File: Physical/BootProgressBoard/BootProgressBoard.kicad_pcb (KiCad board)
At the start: 2 copper layers, 67.5 x 28.6 mm, 15 parts, among them P1 CONN_01X09

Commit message: Latest version
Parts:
- moved G*** 18.5 mm to (154.4, 61.7)
- moved G*** 18.5 mm to (99.3, 61.7)
- moved P1 5.08 mm to (144.8, 59.7)
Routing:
- net Net-(D1-Pad2): track 23.0 -> 17.9 mm
- net Net-(D2-Pad2): track 16.8 -> 11.8 mm
- net Net-(D8-Pad2): track 7.40 -> 11.9 mm
- net Net-(D7-Pad2): track 6.35 -> 10.2 mm
- net Net-(P1-Pad1): track 45.2 -> 48.9 mm
- net Net-(D3-Pad2): track 13.6 -> 11.1 mm
- net Net-(D4-Pad2): track 11.0 -> 8.67 mm
- net Net-(D6-Pad2): track 7.40 -> 8.67 mm
- net Net-(D5-Pad2): track 8.45 -> 7.62 mm
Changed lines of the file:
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@@
     (thickness 1.6)
     (drawings 13)
-    (tracks 55)
+    (tracks 67)
     (zones 0)
     (modules 15)
@@
   )
   (module "MCQN Ltd:miab-logo-9x7mm" (layer B.Cu)
-    (at 154.432 43.18 180)
+    (at 154.432 61.722 180)
     (fp_text reference G*** (at 0 0 180) (layer B.SilkS) hide
       (effects (font (thickness 0.3)) (justify mirror))
@@
   )
   (module Socket_Strips:Socket_Strip_Straight_1x09 (layer F.Cu)
-    (at 149.86 59.69 180)
+    (at 144.78 59.69 180)
     (descr "Through hole socket strip")
     (tags "socket strip")
@@
   )
   (module "MCQN Ltd:miab-logo-9x7mm" (layer F.Cu)
-    (at 99.314 43.18)
+    (at 99.314 61.722)
     (fp_text reference G*** (at 0 0) (layer F.SilkS) hide
       (effects (font (thickness 0.3)))
@@
     (effects (font (size 1.5 1.5) (thickness 0.3)))
   )
-  (gr_text GND (at 154.432 59.69) (layer F.SilkS)
+  (gr_text GND (at 149.098 59.182) (layer F.SilkS)
     (effects (font (size 1.5 1.5) (thickness 0.3)))
   )
@@
     (effects (font (size 1.5 1.5) (thickness 0.3)))
   )
-  (gr_text bpb20170406 (at 99.822 64.262) (layer F.SilkS)
+  (gr_text bpb20170406 (at 153.924 61.976) (layer F.SilkS)
     (effects (font (size 1 1) (thickness 0.25)))
   )
@@
   (gr_line (start 160.67 39.1) (end 160.67 65.675) (layer Edge.Cuts) (width 0.15))
   (gr_line (start 94.14 38.1) (end 159.67 38.1) (layer Edge.Cuts) (width 0.15))
-  (segment (start 129.54 59.69) (end 115.57 59.69) (width 0.3) (layer F.Cu) (net 1))
-  (segment (start 115.57 59.69) (end 109.22 53.34) (width 0.3) (layer F.Cu) (net 1))
+  (segment (start 124.46 59.69) (end 115.57 59.69) (width 0.3) (layer F.Cu) (net 1))
+  (segment (start 115.57 59.69) (end 114.3 58.42) (width 0.3) (layer F.Cu) (net 1))
+  (segment (start 114.3 58.42) (end 109.22 53.34) (width 0.3) (layer F.Cu) (net 1))
   (segment (start 106.8 43.18) (end 106.8 53.22) (width 0.3) (layer F.Cu) (net 2))
   (segment (start 106.8 53.22) (end 106.68 53.34) (width 0.3) (layer F.Cu) (net 2))
@@
   (segment (start 129.54 45.72) (end 129.54 45.8724) (width 0.3) (layer F.Cu) (net 3))
   (segment (start 129.54 45.8724) (end 127.1524 48.26) (width 0.3) (layer F.Cu) (net 3))
-  (segment (start 132.08 59.69) (end 129.54 57.15) (width 0.3) (layer F.Cu) (net 4))
-  (segment (start 129.54 57.15) (end 120.65 57.15) (width 0.3) (layer F.Cu) (net 4))
-  (segment (start 120.65 57.15) (end 119.38 55.88) (width 0.3) (layer F.Cu) (net 4))
+  (segment (start 127 59.69) (end 127 59.5376) (width 0.3) (layer F.Cu) (net 4))
+  (segment (start 127 59.5376) (end 124.968 57.5056) (width 0.3) (layer F.Cu) (net 4))
+  (segment (start 124.968 57.5056) (end 121.0056 57.5056) (width 0.3) (layer F.Cu) (net 4))
+  (segment (start 121.0056 57.5056) (end 119.38 55.88) (width 0.3) (layer F.Cu) (net 4))
   (segment (start 119.38 55.88) (end 119.38 53.34) (width 0.3) (layer F.Cu) (net 4))
   (segment (start 125.73 49.53) (end 121.92 53.34) (width 0.3) (layer F.Cu) (net 5))
@@
   (segment (start 132.08 45.8724) (end 128.4224 49.53) (width 0.3) (layer F.Cu) (net 5))
   (segment (start 132.08 45.72) (end 132.08 45.8724) (width 0.3) (layer F.Cu) (net 5))
+  (segment (start 129.54 59.69) (end 129.54 58.374) (width 0.3) (layer F.Cu) (net 6))
+  (segment (start 129.54 58.374) (end 127.554 56.388) (width 0.3) (layer F.Cu) (net 6))
+  (segment (start 125.476 56.388) (end 124.46 55.372) (width 0.3) (layer F.Cu) (net 6))
+  (segment (start 127.554 56.388) (end 125.476 56.388) (width 0.3) (layer F.Cu) (net 6))
+  (segment (start 124.46 55.372) (end 124.46 53.34) (width 0.3) (layer F.Cu) (net 6))
+  (segment (start 129.54 59.69) (end 129.54 59.5376) (width 0.3) (layer F.Cu) (net 6))
   (segment (start 124.46 54.61) (end 124.46 53.34) (width 0.3) (layer F.Cu) (net 6))
-  (segment (start 125.73 55.88) (end 124.46 54.61) (width 0.3) (layer F.Cu) (net 6))
-  (segment (start 129.54 55.88) (end 125.73 55.88) (width 0.3) (layer F.Cu) (net 6))
-  (segment (start 130.81 57.15) (end 129.54 55.88) (width 0.3) (layer F.Cu) (net 6))
-  (segment (start 132.2324 57.15) (end 130.81 57.15) (width 0.3) (layer F.Cu) (net 6))
-  (segment (start 134.62 59.69) (end 134.62 59.5376) (width 0.3) (layer F.Cu) (net 6))
-  (segment (start 134.62 59.5376) (end 132.2324 57.15) (width 0.3) (layer F.Cu) (net 6))
   (segment (start 134.62 45.72) (end 134.62 45.8724) (width 0.3) (layer F.Cu) (net 7))
   (segment (start 134.62 45.8724) (end 127.1524 53.34) (width 0.3) (layer F.Cu) (net 7))
   (segment (start 127.1524 53.34) (end 127 53.34) (width 0.3) (layer F.Cu) (net 7))
-  (segment (start 133.35 55.88) (end 137.16 59.69) (width 0.3) (layer F.Cu) (net 8))
-  (segment (start 130.81 55.88) (end 133.35 55.88) (width 0.3) (layer F.Cu) (net 8))
-  (segment (start 129.54 54.61) (end 130.81 55.88) (width 0.3) (layer F.Cu) (net 8))
+  (segment (start 132.08 59.69) (end 132.08 57.912) (width 0.3) (layer F.Cu) (net 8))
+  (segment (start 132.08 57.912) (end 129.54 55.372) (width 0.3) (layer F.Cu) (net 8))
+  (segment (start 129.54 55.372) (end 129.54 53.34) (width 0.3) (layer F.Cu) (net 8))
   (segment (start 129.54 53.34) (end 129.54 54.61) (width 0.3) (layer F.Cu) (net 8))
   (segment (start 137.16 45.72) (end 137.16 45.8724) (width 0.3) (layer F.Cu) (net 9))
   (segment (start 137.16 45.8724) (end 132.08 50.9524) (width 0.3) (layer F.Cu) (net 9))
   (segment (start 132.08 50.9524) (end 132.08 53.34) (width 0.3) (layer F.Cu) (net 9))
-  (segment (start 134.62 54.61) (end 139.7 59.69) (width 0.3) (layer F.Cu) (net 10))
+  (segment (start 134.62 59.69) (end 134.62 53.34) (width 0.3) (layer F.Cu) (net 10))
   (segment (start 134.62 53.34) (end 134.62 54.61) (width 0.3) (layer F.Cu) (net 10))
   (segment (start 137.16 50.8) (end 137.16 53.34) (width 0.3) (layer F.Cu) (net 11))
   (segment (start 139.7 48.26) (end 137.16 50.8) (width 0.3) (layer F.Cu) (net 11))
   (segment (start 139.7 45.72) (end 139.7 48.26) (width 0.3) (layer F.Cu) (net 11))
-  (segment (start 142.24 57.15) (end 142.24 59.69) (width 0.3) (layer F.Cu) (net 12))
-  (segment (start 139.7 54.61) (end 142.24 57.15) (width 0.3) (layer F.Cu) (net 12))
+  (segment (start 137.16 59.69) (end 137.16 57.658) (width 0.3) (layer F.Cu) (net 12))
+  (segment (start 137.16 57.658) (end 139.7 55.118) (width 0.3) (layer F.Cu) (net 12))
+  (segment (start 139.7 55.118) (end 139.7 53.34) (width 0.3) (layer F.Cu) (net 12))
   (segment (start 139.7 53.34) (end 139.7 54.61) (width 0.3) (layer F.Cu) (net 12))
   (segment (start 142.24 45.72) (end 142.24 53.34) (width 0.3) (layer F.Cu) (net 13))
-  (segment (start 144.78 53.34) (end 144.78 59.69) (width 0.3) (layer F.Cu) (net 14))
+  (segment (start 139.7 57.912) (end 140.716 56.896) (width 0.3) (layer F.Cu) (net 14))
+  (segment (start 140.716 56.896) (end 140.97 56.642) (width 0.3) (layer F.Cu) (net 14))
+  (segment (start 144.78 53.34) (end 144.78 55.118) (width 0.3) (layer F.Cu) (net 14))
+  (segment (start 144.78 55.118) (end 144.272 55.626) (width 0.3) (layer F.Cu) (net 14))
+  (segment (start 144.272 55.626) (end 141.986 55.626) (width 0.3) (layer F.Cu) (net 14))
+  (segment (start 141.986 55.626) (end 140.716 56.896) (width 0.3) (layer F.Cu) (net 14))
+  (segment (start 139.7 59.69) (end 139.7 57.912) (width 0.3) (layer F.Cu) (net 14))
   (segment (start 147.32 50.8) (end 147.32 53.34) (width 0.3) (layer F.Cu) (net 15))
   (segment (start 144.78 48.26) (end 147.32 50.8) (width 0.3) (layer F.Cu) (net 15))
   (segment (start 144.78 45.72) (end 144.78 48.26) (width 0.3) (layer F.Cu) (net 15))
-  (segment (start 147.32 57.15) (end 147.32 59.69) (width 0.3) (layer F.Cu) (net 16))
-  (segment (start 149.86 54.61) (end 147.32 57.15) (width 0.3) (layer F.Cu) (net 16))
-  (segment (start 149.86 53.34) (end 149.86 54.61) (width 0.3) (layer F.Cu) (net 16))
-  (segment (start 152.4 57.15) (end 149.86 59.69) (width 0.3) (layer F.Cu) (net 18))
-  (segment (start 152.4 48.26) (end 152.4 57.15) (width 0.3) (layer F.Cu) (net 18))
-  (segment (start 149.86 45.72) (end 152.4 48.26) (width 0.3) (layer F.Cu) (net 18))
-  (segment (start 147.32 45.72) (end 149.86 45.72) (width 0.3) (layer F.Cu) (net 18))
+  (segment (start 142.24 59.69) (end 142.24 58.166) (width 0.3) (layer F.Cu) (net 16))
+  (segment (start 142.24 58.166) (end 143.256 57.15) (width 0.3) (layer F.Cu) (net 16))
+  (segment (start 143.256 57.15) (end 147.32 57.15) (width 0.3) (layer F.Cu) (net 16))
+  (segment (start 147.32 57.15) (end 149.86 54.61) (width 0.3) (layer F.Cu) (net 16))
+  (segment (start 149.86 54.61) (end 149.86 53.34) (width 0.3) (layer F.Cu) (net 16))
+  (segment (start 144.78 59.69) (end 147.574 59.69) (width 0.3) (layer F.Cu) (net 18))
+  (segment (start 152.4 54.864) (end 152.4 48.26) (width 0.3) (layer F.Cu) (net 18))
+  (segment (start 147.574 59.69) (end 152.4 54.864) (width 0.3) (layer F.Cu) (net 18))
+  (segment (start 152.4 48.26) (end 149.86 45.72) (width 0.3) (layer F.Cu) (net 18))
+  (segment (start 149.86 45.72) (end 147.32 45.72) (width 0.3) (layer F.Cu) (net 18))
   (segment (start 144.78 43.18) (end 147.32 45.72) (width 0.3) (layer F.Cu) (net 18))
   (segment (start 121.8 43.18) (end 144.78 43.18) (width 0.3) (layer F.Cu) (net 18))

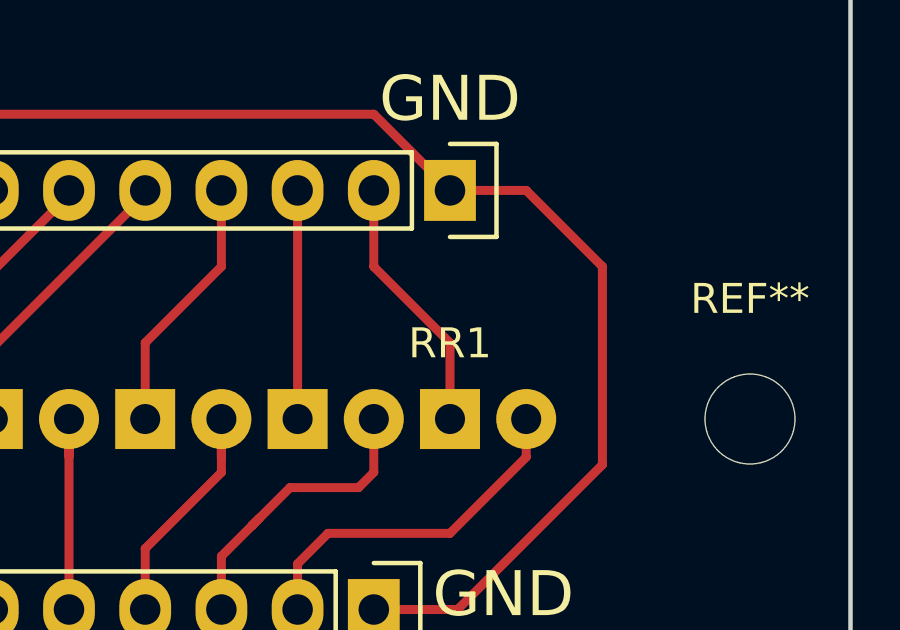
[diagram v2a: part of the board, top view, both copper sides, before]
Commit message: Add logo to the Boomer amp.  Part of #86
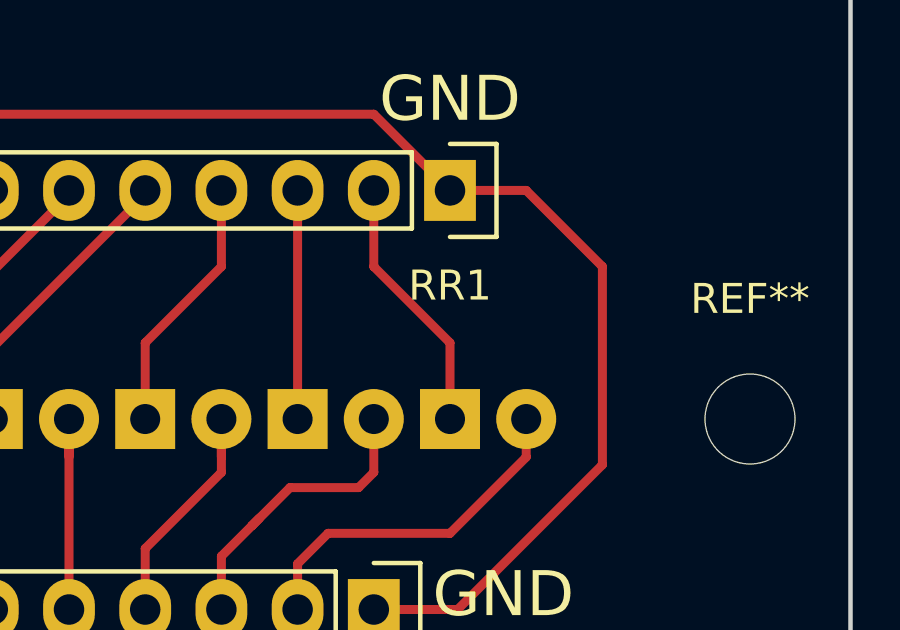
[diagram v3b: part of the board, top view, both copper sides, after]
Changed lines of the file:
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@@
-(kicad_pcb (version 20170123) (host pcbnew no-vcs-found-1e25c47~58~ubuntu16.04.1)
+(kicad_pcb (version 20171130) (host pcbnew 5.0.1-33cea8e~67~ubuntu18.04.1)
   (general
-    (links 18)
-    (no_connects 0)
-    (area 90.191475 38.024999 165.810046 66.750001)
     (thickness 1.6)
     (drawings 13)
@@
     (pad_drill 0.762)
     (pad_to_mask_clearance 0.2)
+    (solder_mask_min_width 0.25)
     (aux_axis_origin 0 0)
     (visible_elements FFFFFF7F)
@@
       (layerselection 0x010fc_ffffffff)
       (usegerberextensions false)
+      (usegerberattributes false)
+      (usegerberadvancedattributes false)
+      (creategerberjobfile false)
       (excludeedgelayer true)
       (linewidth 0.100000)
@@
       (hpglpennumber 1)
       (hpglpenspeed 20)
-      (hpglpendiameter 15)
+      (hpglpendiameter 15.000000)
       (psnegative false)
       (psa4output false)
@@
       (drillshape 0)
       (scaleselection 1)
-      (outputdirectory /home/adrian/sandbox/github/brain/Physical/BootProgressBoard/Output/))
+      (outputdirectory "/home/adrian/sandbox/github/brain/Physical/BootProgressBoard/Output/"))
   )
   (net 0 "")
@@
     (at 154.432 61.722 180)
     (fp_text reference G*** (at 0 0 180) (layer B.SilkS) hide
-      (effects (font (thickness 0.3)) (justify mirror))
+      (effects (font (size 1.524 1.524) (thickness 0.3)) (justify mirror))
     )
     (fp_text value LOGO (at 0.75 0 180) (layer B.SilkS) hide
-      (effects (font (thickness 0.3)) (justify mirror))
+      (effects (font (size 1.524 1.524) (thickness 0.3)) (justify mirror))
     )
     (fp_poly (pts (xy 4.611512 -3.293533) (xy -4.608688 -3.293533) (xy -4.608688 -1.255324) (xy -3.7846 -1.255324)
@@
       (net 4 "Net-(D2-Pad2)"))
     (model LEDs.3dshapes/LED-3MM.wrl
-      (at (xyz 0.05 0 0))
+      (offset (xyz 1.269999980926514 0 0))
       (scale (xyz 1 1 1))
       (rotate (xyz 0 0 90))
@@
       (net 6 "Net-(D3-Pad2)"))
     (model LEDs.3dshapes/LED-3MM.wrl
-      (at (xyz 0.05 0 0))
+      (offset (xyz 1.269999980926514 0 0))
       (scale (xyz 1 1 1))
       (rotate (xyz 0 0 90))
@@
       (net 8 "Net-(D4-Pad2)"))
     (model LEDs.3dshapes/LED-3MM.wrl
-      (at (xyz 0.05 0 0))
+      (offset (xyz 1.269999980926514 0 0))
       (scale (xyz 1 1 1))
       (rotate (xyz 0 0 90))
@@
       (net 10 "Net-(D5-Pad2)"))
     (model LEDs.3dshapes/LED-3MM.wrl
-      (at (xyz 0.05 0 0))
+      (offset (xyz 1.269999980926514 0 0))
       (scale (xyz 1 1 1))
       (rotate (xyz 0 0 90))
@@
       (net 12 "Net-(D6-Pad2)"))
     (model LEDs.3dshapes/LED-3MM.wrl
-      (at (xyz 0.05 0 0))
+      (offset (xyz 1.269999980926514 0 0))
       (scale (xyz 1 1 1))
       (rotate (xyz 0 0 90))
@@
       (net 14 "Net-(D7-Pad2)"))
     (model LEDs.3dshapes/LED-3MM.wrl
-      (at (xyz 0.05 0 0))
+      (offset (xyz 1.269999980926514 0 0))
       (scale (xyz 1 1 1))
       (rotate (xyz 0 0 90))
@@
       (net 16 "Net-(D8-Pad2)"))
     (model LEDs.3dshapes/LED-3MM.wrl
-      (at (xyz 0.05 0 0))
+      (offset (xyz 1.269999980926514 0 0))
       (scale (xyz 1 1 1))
       (rotate (xyz 0 0 90))
@@
       (net 1 "Net-(D1-Pad2)"))
     (model Socket_Strips.3dshapes/Socket_Strip_Straight_1x09.wrl
-      (at (xyz 0.4 0 0))
+      (offset (xyz 10.15999984741211 0 0))
       (scale (xyz 1 1 1))
       (rotate (xyz 0 0 180))
@@
     (descr "Through hole socket strip")
     (tags "socket strip")
-    (fp_text reference RR1 (at 0 -5.1 180) (layer F.SilkS)
+    (fp_text reference RR1 (at 0 -3.175 180) (layer F.SilkS)
       (effects (font (size 1 1) (thickness 0.15)))
     )
@@
       (net 17 "Net-(RR1-Pad9)"))
     (model Socket_Strips.3dshapes/Socket_Strip_Straight_1x09.wrl
-      (at (xyz 0.4 0 0))
+      (offset (xyz 10.15999984741211 0 0))
       (scale (xyz 1 1 1))
       (rotate (xyz 0 0 180))
@@
     (at 99.314 61.722)
     (fp_text reference G*** (at 0 0) (layer F.SilkS) hide
-      (effects (font (thickness 0.3)))
+      (effects (font (size 1.524 1.524) (thickness 0.3)))
     )
     (fp_text value LOGO (at 0.75 0) (layer F.SilkS) hide
-      (effects (font (thickness 0.3)))
+      (effects (font (size 1.524 1.524) (thickness 0.3)))
     )
     (fp_poly (pts (xy 4.611512 3.293533) (xy -4.608688 3.293533) (xy -4.608688 1.255324) (xy -3.7846 1.255324)
